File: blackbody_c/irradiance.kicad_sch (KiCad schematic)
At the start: 11 parts, among them J2 Conn_01x05_Pin, U2 LTC4316IMS-PBF

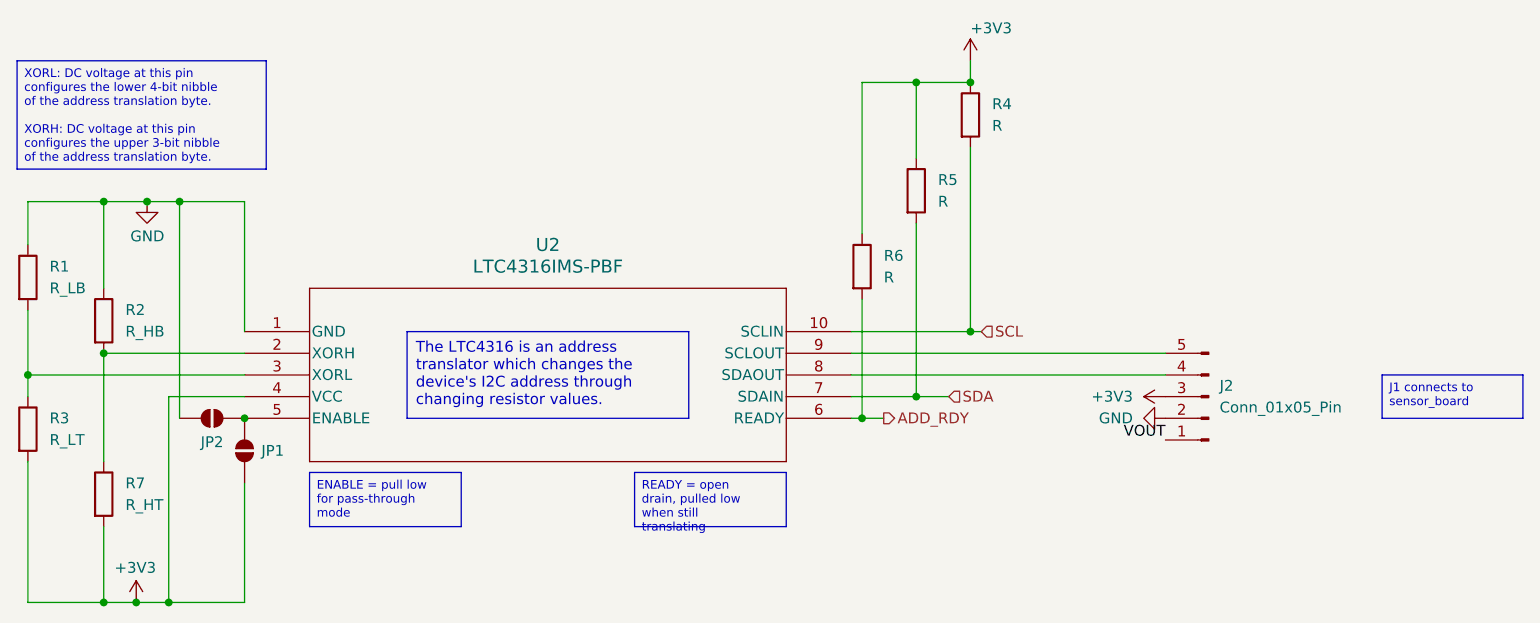
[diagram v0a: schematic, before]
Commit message: added more complexity + thermistor connection
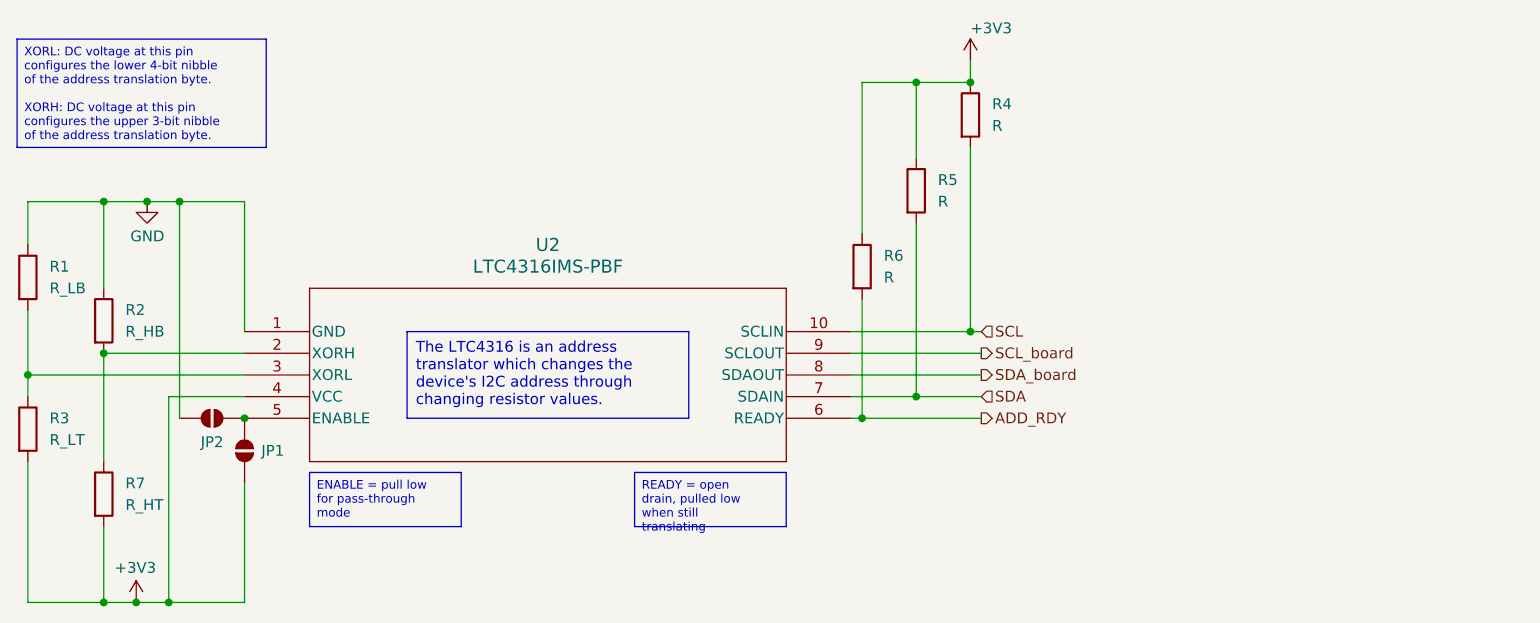
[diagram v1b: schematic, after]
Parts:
- removed J2: Conn_01x05_Pin, symbol Connector:Conn_01x05_Pin
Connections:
- net SDA_board: now reaches U2.8 (SDAOUT)
- net SCL_board: now reaches U2.9 (SCLOUT)

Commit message: Initial version of sensor communication through all three boards
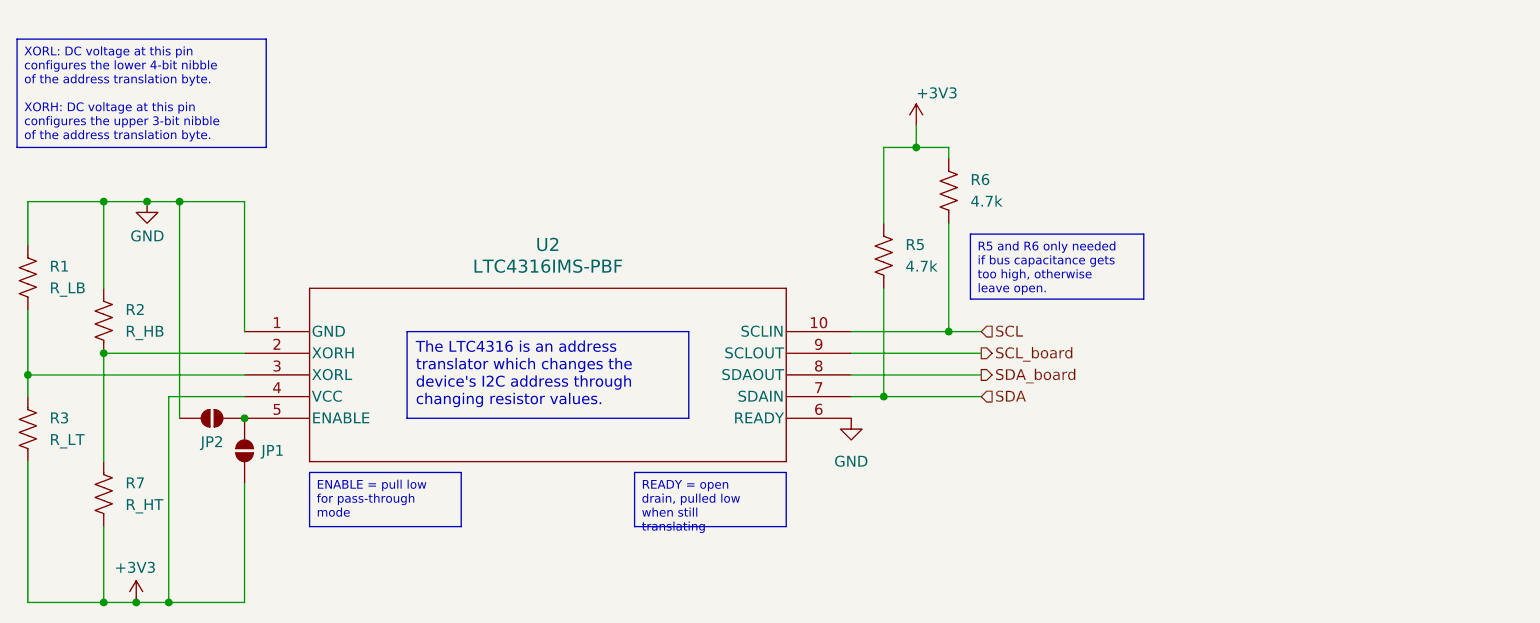
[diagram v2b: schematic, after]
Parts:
- removed R1: R_LB, symbol Device:R
- removed R2: R_HB, symbol Device:R
- removed R3: R_LT, symbol Device:R
- removed R4, R5, R6: R, symbol Device:R
- removed R7: R_HT, symbol Device:R
- added R1: R_LB, symbol Device:R_US
- added R2: R_HB, symbol Device:R_US
- added R3: R_LT, symbol Device:R_US
- added R5, R6: 4.7k, symbol Device:R_US
- added R7: R_HT, symbol Device:R_US
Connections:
- net ADD_RDY is gone; now on net GND: U2.6 (READY)
- net +3V3: now also R3.2, R5.1, R6.1, R7.2
- net GND: now also R1.1, R2.1
- net SCL: now also R6.2
- net SDA: now also R5.2
- net at U2.3 (XORL): now also R1.2, R3.1
- net at U2.2 (XORH): now also R2.2, R7.1

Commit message: Updated minor errors
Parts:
- renumbered R7 to R4
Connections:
- net GND: no longer U2.6 (READY)
- no-connect marks 0 -> 1
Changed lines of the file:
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@@
 		(color 0 0 0 0)
+	)
+	(no_connect
+		(at 134.62 86.36)
 	)
 	(wire
@@
 		)
 	)
-	(text_box "READY = open drain, pulled low when still translating\n"
-		(exclude_from_sim no)
-		(at 109.22 92.71 0)
-		(size 17.78 6.35)
+	(text_box "READY = signals when address translation is finished, leave open if unused\n"
+		(exclude_from_sim no)
+		(at 107.95 92.71 0)
+		(size 19.05 7.62)
 		(stroke
 			(width 0)
@@
 	)
 	(symbol
-		(lib_id "power:GND")
-		(at 134.62 86.36 0)
-		(unit 1)
-		(exclude_from_sim no)
-		(in_bom yes)
-		(on_board yes)
-		(dnp no)
-		(fields_autoplaced yes)
-		(property "Reference" "#PWR08"
-			(at 134.62 92.71 0)
-			(effects
-				(font
-					(size 1.27 1.27)
-				)
-				(hide yes)
-			)
-		)
-		(property "Value" "GND"
-			(at 134.62 91.44 0)
-			(effects
-				(font
-					(size 1.27 1.27)
-				)
-			)
-		)
-		(property "Footprint" ""
-			(at 134.62 86.36 0)
-			(effects
-				(font
-					(size 1.27 1.27)
-				)
-				(hide yes)
-			)
-		)
-		(property "Datasheet" ""
-			(at 134.62 86.36 0)
-			(effects
-				(font
-					(size 1.27 1.27)
-				)
-				(hide yes)
-			)
-		)
-		(property "Description" "Power symbol creates a global label with name \"GND\" , ground"
-			(at 134.62 86.36 0)
-			(effects
-				(font
-					(size 1.27 1.27)
-				)
-				(hide yes)
-			)
-		)
-		(pin "1"
-		)
-		(instances
-			(project ""
-				(path "/15ea72e6-1a84-45bd-8e41-b7984e09a4da/ddefad2e-848c-4145-b4aa-774f2135e64c"
-					(reference "#PWR08")
-					(unit 1)
-				)
-			)
-		)
-	)
-	(symbol
 		(lib_id "Device:R_US")
 		(at 38.1 87.63 0)
@@
 			)
 		)
-		(property "Datasheet" "LTC4316IMS-PBF"
+		(property "Datasheet" "https://cdn-learn.adafruit.com/assets/assets/000/129/112/original/4316fa.pdf?1712063113"
 			(at 63.5 76.2 0)
 			(effects
@@
 		(dnp no)
 		(fields_autoplaced yes)
-		(property "Reference" "R7"
+		(property "Reference" "R4"
 			(at 49.53 93.9799 0)
 			(effects
@@
 			(project "blackbody_c"
 				(path "/15ea72e6-1a84-45bd-8e41-b7984e09a4da/ddefad2e-848c-4145-b4aa-774f2135e64c"
-					(reference "R7")
+					(reference "R4")
 					(unit 1)
 				)

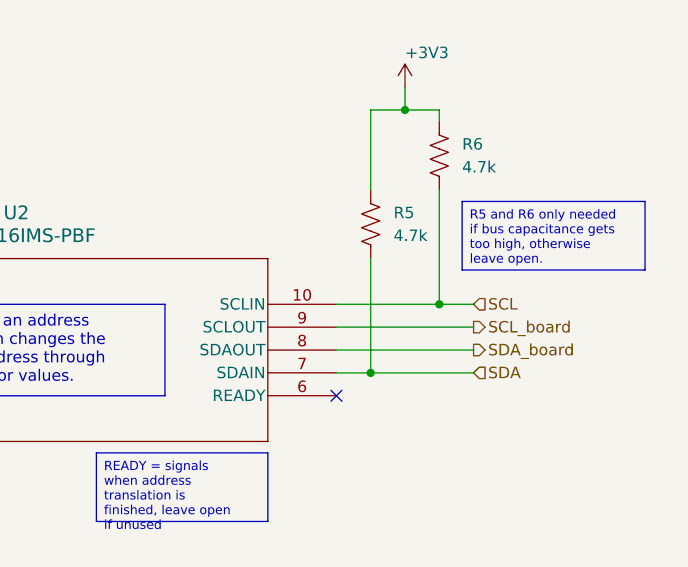
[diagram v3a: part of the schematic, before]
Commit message: Added controller and CAN
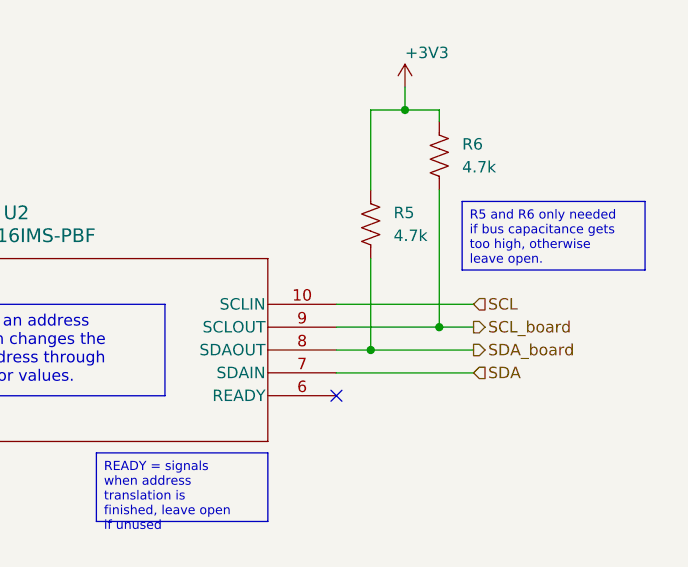
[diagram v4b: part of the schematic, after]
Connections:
- net SCL: no longer R6.2
- net SCL_board: now also R6.2
- net SDA: no longer R5.2
- net SDA_board: now also R5.2
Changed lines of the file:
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@@
 	(paper "A4")
 	(junction
-		(at 146.05 76.2)
-		(diameter 0)
-		(color 0 0 0 0)
-	)
-	(junction
 		(at 52.07 60.96)
 		(diameter 0)
@@
 	)
 	(junction
-		(at 138.43 83.82)
-		(diameter 0)
-		(color 0 0 0 0)
-	)
-	(junction
 		(at 54.61 107.95)
 		(diameter 0)
@@
 	)
 	(junction
+		(at 146.05 78.74)
+		(diameter 0)
+		(color 0 0 0 0)
+	)
+	(junction
 		(at 46.99 78.74)
 		(diameter 0)
@@
 	(junction
 		(at 38.1 81.28)
+		(diameter 0)
+		(color 0 0 0 0)
+	)
+	(junction
+		(at 138.43 81.28)
 		(diameter 0)
 		(color 0 0 0 0)
@@
 	(wire
 		(pts
-			(xy 146.05 76.2) (xy 149.86 76.2)
-		)
-		(stroke
-			(width 0)
-			(type default)
-		)
-	)
-	(wire
-		(pts
 			(xy 38.1 81.28) (xy 38.1 83.82)
 		)
@@
 	(wire
 		(pts
-			(xy 134.62 83.82) (xy 138.43 83.82)
+			(xy 134.62 83.82) (xy 149.86 83.82)
 		)
 		(stroke
@@
 	(wire
 		(pts
-			(xy 146.05 63.5) (xy 146.05 76.2)
-		)
-		(stroke
-			(width 0)
-			(type default)
-		)
-	)
-	(wire
-		(pts
 			(xy 55.88 60.96) (xy 55.88 86.36)
 		)
@@
 	(wire
 		(pts
-			(xy 138.43 71.12) (xy 138.43 83.82)
-		)
-		(stroke
-			(width 0)
-			(type default)
-		)
-	)
-	(wire
-		(pts
 			(xy 50.8 107.95) (xy 54.61 107.95)
 		)
@@
 	(wire
 		(pts
+			(xy 146.05 78.74) (xy 149.86 78.74)
+		)
+		(stroke
+			(width 0)
+			(type default)
+		)
+	)
+	(wire
+		(pts
 			(xy 38.1 60.96) (xy 38.1 66.04)
 		)
@@
 	(wire
 		(pts
-			(xy 138.43 83.82) (xy 149.86 83.82)
+			(xy 138.43 71.12) (xy 138.43 81.28)
 		)
 		(stroke
@@
 	(wire
 		(pts
-			(xy 134.62 78.74) (xy 149.86 78.74)
+			(xy 134.62 78.74) (xy 146.05 78.74)
 		)
 		(stroke
@@
 	(wire
 		(pts
+			(xy 146.05 63.5) (xy 146.05 78.74)
+		)
+		(stroke
+			(width 0)
+			(type default)
+		)
+	)
+	(wire
+		(pts
 			(xy 63.5 93.98) (xy 63.5 107.95)
 		)
@@
 	(wire
 		(pts
-			(xy 134.62 76.2) (xy 146.05 76.2)
+			(xy 134.62 76.2) (xy 149.86 76.2)
 		)
 		(stroke
@@
 	(wire
 		(pts
-			(xy 134.62 81.28) (xy 149.86 81.28)
+			(xy 134.62 81.28) (xy 138.43 81.28)
 		)
 		(stroke
@@
 		)
 		(stroke
+			(width 0)
+			(type default)
+		)
+	)
+	(wire
+		(pts
+			(xy 138.43 81.28) (xy 149.86 81.28)
+		)
+		(stroke

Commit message: layout iteration 1
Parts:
- JP1, JP2: footprint (none) -> Jumper:SolderJumper-2_P1.3mm_Open_RoundedPad1.0x1.5mm
- R1, R2, R3, R4, R5, R6: footprint (none) -> Resistor_SMD:R_0805_2012Metric
- U2: footprint MSOP-10_MS_LIT -> blackbody_c:MSOP-10_MS_LIT
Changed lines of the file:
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@@
 (kicad_sch
-	(version 20231120)
+	(version 20250114)
 	(generator "eeschema")
-	(generator_version "8.0")
+	(generator_version "9.0")
 	(paper "A4")
+	(text_box "The LTC4316 is an address translator which changes the device's I2C address through changing resistor values."
+		(exclude_from_sim no)
+		(at 82.55 76.2 0)
+		(size 33.02 10.16)
+		(margins 0.9525 0.9525 0.9525 0.9525)
+		(stroke
+			(width 0)
+			(type default)
+		)
+		(fill
+			(type none)
+		)
+		(effects
+			(font
+				(size 1.27 1.27)
+			)
+			(justify left top)
+		)
+	)
+	(text_box "READY = signals when address translation is finished, leave open if unused\n"
+		(exclude_from_sim no)
+		(at 107.95 92.71 0)
+		(size 19.05 7.62)
+		(margins 0.762 0.762 0.762 0.762)
+		(stroke
+			(width 0)
+			(type default)
+		)
+		(fill
+			(type none)
+		)
+		(effects
+			(font
+				(size 1.016 1.016)
+			)
+			(justify left top)
+		)
+	)
+	(text_box "R5 and R6 only needed if bus capacitance gets too high, otherwise leave open."
+		(exclude_from_sim no)
+		(at 148.59 64.77 0)
+		(size 20.32 7.62)
+		(margins 0.762 0.762 0.762 0.762)
+		(stroke
+			(width 0)
+			(type default)
+		)
+		(fill
+			(type none)
+		)
+		(effects
+			(font
+				(size 1.016 1.016)
+			)
+			(justify left top)
+		)
+	)
+	(text_box "ENABLE = pull low for pass-through mode\n"
+		(exclude_from_sim no)
+		(at 71.12 92.71 0)
+		(size 17.78 6.35)
+		(margins 0.762 0.762 0.762 0.762)
+		(stroke
+			(width 0)
+			(type default)
+		)
+		(fill
+			(type none)
+		)
+		(effects
+			(font
+				(size 1.016 1.016)
+			)
+			(justify left top)
+		)
+	)
+	(text_box "XORL: DC voltage at this pin configures the lower 4-bit nibble of the address translation byte.\n\nXORH: DC voltage at this pin configures the upper 3-bit nibble of the address translation byte."
+		(exclude_from_sim no)
+		(at 36.83 41.91 0)
+		(size 29.21 12.7)
+		(margins 0.762 0.762 0.762 0.762)
+		(stroke
+			(width 0)
+			(type default)
+		)
+		(fill
+			(type none)
+		)
+		(effects
+			(font
+				(size 1.016 1.016)
+			)
+			(justify left top)
+		)
+	)
 	(junction
 		(at 52.07 60.96)
@@
 		)
 	)
-	(text_box "The LTC4316 is an address translator which changes the device's I2C address through changing resistor values."
-		(exclude_from_sim no)
-		(at 82.55 76.2 0)
-		(size 33.02 10.16)
-		(stroke
-			(width 0)
-			(type default)
-		)
-		(fill
-			(type none)
-		)
+	(hierarchical_label "SCL_board"
+		(shape output)
+		(at 149.86 78.74 0)
 		(effects
 			(font
 				(size 1.27 1.27)
 			)
-			(justify left top)
-		)
-	)
-	(text_box "READY = signals when address translation is finished, leave open if unused\n"
-		(exclude_from_sim no)
-		(at 107.95 92.71 0)
-		(size 19.05 7.62)
-		(stroke
-			(width 0)
-			(type default)
-		)
-		(fill
-			(type none)
-		)
-		(effects
-			(font
-				(size 1.016 1.016)
-			)
-			(justify left top)
-		)
-	)
-	(text_box "R5 and R6 only needed if bus capacitance gets too high, otherwise leave open."
-		(exclude_from_sim no)
-		(at 148.59 64.77 0)
-		(size 20.32 7.62)
-		(stroke
-			(width 0)
-			(type default)
-		)
-		(fill
-			(type none)
-		)
-		(effects
-			(font
-				(size 1.016 1.016)
-			)
-			(justify left top)
-		)
-	)
-	(text_box "ENABLE = pull low for pass-through mode\n"
-		(exclude_from_sim no)
-		(at 71.12 92.71 0)
-		(size 17.78 6.35)
-		(stroke
-			(width 0)
-			(type default)
-		)
-		(fill
-			(type none)
-		)
-		(effects
-			(font
-				(size 1.016 1.016)
-			)
-			(justify left top)
-		)
-	)
-	(text_box "XORL: DC voltage at this pin configures the lower 4-bit nibble of the address translation byte.\n\nXORH: DC voltage at this pin configures the upper 3-bit nibble of the address translation byte."
-		(exclude_from_sim no)
-		(at 36.83 41.91 0)
-		(size 29.21 12.7)
-		(stroke
-			(width 0)
-			(type default)
-		)
-		(fill
-			(type none)
-		)
-		(effects
-			(font
-				(size 1.016 1.016)
-			)
-			(justify left top)
-		)
-	)
-	(hierarchical_label "SCL_board"
-		(shape output)
-		(at 149.86 78.74 0)
-		(fields_autoplaced yes)
+			(justify left)
+		)
+	)
+	(hierarchical_label "SCL"
+		(shape input)
+		(at 149.86 76.2 0)
 		(effects
 			(font
@@
 		)
 	)
-	(hierarchical_label "SCL"
+	(hierarchical_label "SDA"
 		(shape input)
-		(at 149.86 76.2 0)
-		(fields_autoplaced yes)
+		(at 149.86 83.82 0)
 		(effects
 			(font
@@
 		)
 	)
-	(hierarchical_label "SDA"
-		(shape input)
-		(at 149.86 83.82 0)
-		(fields_autoplaced yes)
-		(effects
-			(font
-				(size 1.27 1.27)
-			)
-			(justify left)
-		)
-	)
 	(hierarchical_label "SDA_board"
 		(shape output)
 		(at 149.86 81.28 0)
-		(fields_autoplaced yes)
 		(effects
 			(font
@@
 			)
 		)
-		(property "Footprint" ""
+		(property "Footprint" "Resistor_SMD:R_0805_2012Metric"
 			(at 39.116 87.884 90)
 			(effects
@@
 			)
 		)
-		(property "Footprint" ""
+		(property "Footprint" "Resistor_SMD:R_0805_2012Metric"
 			(at 48.006 75.184 90)
 			(effects
@@
 			)
 		)
-		(property "Footprint" ""
+		(property "Footprint" "Resistor_SMD:R_0805_2012Metric"
 			(at 39.116 70.104 90)
 			(effects
@@
 			)
 		)
-		(property "Footprint" ""
+		(property "Footprint" "Resistor_SMD:R_0805_2012Metric"
 			(at 139.446 67.564 90)
 			(effects
@@
 			)
 		)
-		(property "Footprint" "MSOP-10_MS_LIT"
+		(property "Footprint" "blackbody_c:MSOP-10_MS_LIT"
 			(at 63.5 76.2 0)
 			(effects
@@
 			)
 		)
-		(property "Footprint" ""
+		(property "Footprint" "Jumper:SolderJumper-2_P1.3mm_Open_RoundedPad1.0x1.5mm"
 			(at 59.69 86.36 0)
 			(effects
@@
 			)
 		)
-		(property "Footprint" ""
+		(property "Footprint" "Jumper:SolderJumper-2_P1.3mm_Open_RoundedPad1.0x1.5mm"
 			(at 63.5 90.17 0)
 			(effects
@@
 			)
 		)
-		(property "Footprint" ""
+		(property "Footprint" "Resistor_SMD:R_0805_2012Metric"
 			(at 147.066 59.944 90)
 			(effects
@@
 			)
 		)
-		(property "Footprint" ""
+		(property "Footprint" "Resistor_SMD:R_0805_2012Metric"
 			(at 48.006 95.504 90)
 			(effects
